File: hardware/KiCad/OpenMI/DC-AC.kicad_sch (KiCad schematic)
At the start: 41 parts, among them Q2 IPL60R125P7, Q3 IPL60R125P7, U1 IRS2304S

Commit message: chore: sync library
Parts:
- L10: footprint OpenCE:L_Radial_D10.5mm_P5.00mm_H14.5mm_Wuerth_1014 -> OpenCE:L_Radial_D10.0mm_P5.00mm_H14.0mm_Wuerth_1014
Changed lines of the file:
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@@
       (effects (font (size 1.27 1.27)))
     )
-    (property "Footprint" "OpenCE:L_Radial_D10.5mm_P5.00mm_H14.5mm_Wuerth_1014" (at 208.28 95.25 0)
+    (property "Footprint" "OpenCE:L_Radial_D10.0mm_P5.00mm_H14.0mm_Wuerth_1014" (at 208.28 95.25 0)
       (effects (font (size 1.27 1.27)) hide)
     )

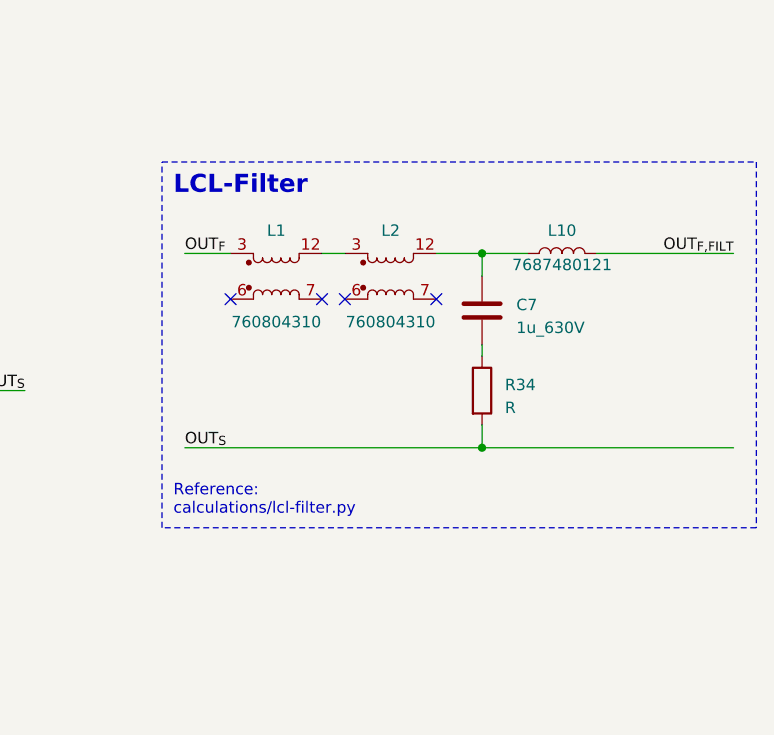
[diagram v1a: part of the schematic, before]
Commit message: feat(hw): Adds damping resistors to LCL-filter
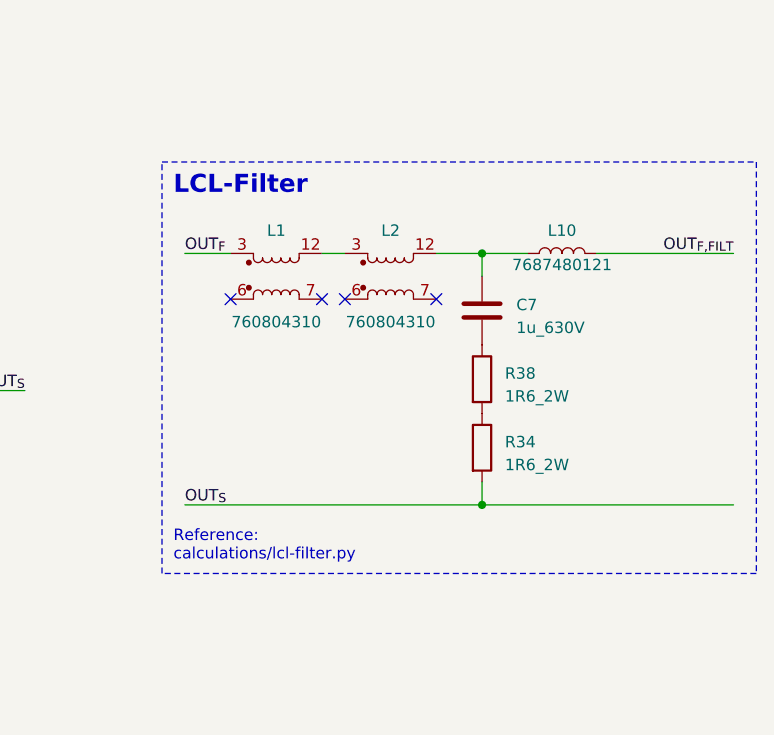
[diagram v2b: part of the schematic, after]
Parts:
- removed R34: R, symbol Device:R
- added R34, R38: 1R6_2W, Resistor_THT:R_Axial_DIN0411_L9.9mm_D3.6mm_P5.08mm_Vertical, symbol _R_Power:1R6_2W
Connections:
- net OUT_{S}: now also R34.2
- net at C7.2: now also R38.1
- new net: R34.1, R38.2
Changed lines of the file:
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@@
   (junction (at 135.89 50.8) (diameter 0) (color 0 0 0 0)
   )
-  (junction (at 199.39 116.84) (diameter 0) (color 0 0 0 0)
+  (junction (at 199.39 123.19) (diameter 0) (color 0 0 0 0)
   )
   (junction (at 93.98 97.79) (diameter 0) (color 0 0 0 0)
@@
     (stroke (width 0) (type default))
   )
-  (wire (pts (xy 166.37 116.84) (xy 199.39 116.84))
+  (wire (pts (xy 166.37 123.19) (xy 199.39 123.19))
     (stroke (width 0) (type default))
   )
@@
     (stroke (width 0) (type default))
   )
-  (wire (pts (xy 199.39 116.84) (xy 227.33 116.84))
+  (wire (pts (xy 199.39 123.19) (xy 227.33 123.19))
     (stroke (width 0) (type default))
   )
@@
     (stroke (width 0) (type default))
   )
-  (wire (pts (xy 199.39 114.3) (xy 199.39 116.84))
-    (stroke (width 0) (type default))
-  )
   (wire (pts (xy 109.22 160.02) (xy 109.22 158.75))
     (stroke (width 0) (type default))
@@
     (stroke (width 0) (type default))
   )
-  (wire (pts (xy 199.39 105.41) (xy 199.39 106.68))
-    (stroke (width 0) (type default))
-  )
   (wire (pts (xy 124.46 172.72) (xy 137.16 172.72))
     (stroke (width 0) (type default))
@@
   )
   (wire (pts (xy 93.98 172.72) (xy 93.98 171.45))
+    (stroke (width 0) (type default))
+  )
+  (wire (pts (xy 199.39 120.65) (xy 199.39 123.19))
     (stroke (width 0) (type default))
   )
@@
     (fill (type none))
   )
-  (rectangle (start 163.83 85.09) (end 229.87 125.73)
+  (rectangle (start 163.83 85.09) (end 229.87 130.81)
     (stroke (width 0) (type dash))
     (fill (type none))
@@
     (effects (font (size 2 2) bold) (justify left bottom))
   )
-  (text "Reference: \ncalculations/lcl-filter.py" (at 165.1 124.46 0)
+  (text "Reference: \ncalculations/lcl-filter.py" (at 165.1 129.54 0)
     (effects (font (size 1.27 1.27)) (justify left bottom))
   )
@@
     (effects (font (size 1.27 1.27) bold) (justify right bottom))
   )
-  (label "OUT_{S}" (at 166.37 116.84 0) (fields_autoplaced)
+  (label "OUT_{S}" (at 166.37 123.19 0) (fields_autoplaced)
     (effects (font (size 1.27 1.27)) (justify left bottom))
   )
@@
         (path "/2d959e19-1572-42a0-a8fd-da8463ad4e66/19323a41-9b99-4de4-bfae-f2f828815be3"
           (reference "R3") (unit 1)
-        )
-      )
-    )
-  )
-  (symbol (lib_id "Device:R") (at 199.39 110.49 0) (unit 1)
-    (in_bom yes) (on_board yes) (dnp no) (fields_autoplaced)
-    (property "Reference" "R34" (at 201.93 109.855 0)
-      (effects (font (size 1.27 1.27)) (justify left))
-    )
-    (property "Value" "R" (at 201.93 112.395 0)
-      (effects (font (size 1.27 1.27)) (justify left))
-    )
-    (property "Footprint" "" (at 197.612 110.49 90)
-      (effects (font (size 1.27 1.27)) hide)
-    )
-    (property "Datasheet" "~" (at 199.39 110.49 0)
-      (effects (font (size 1.27 1.27)) hide)
-    )
-    (pin "1")
-    (pin "2")
-    (instances
-      (project "OpenMI"
-        (path "/2d959e19-1572-42a0-a8fd-da8463ad4e66/19323a41-9b99-4de4-bfae-f2f828815be3"
-          (reference "R34") (unit 1)
         )
       )
@@
     )
   )
+  (symbol (lib_id "_R_Power:1R6_2W") (at 199.39 109.22 0) (unit 1)
+    (in_bom yes) (on_board yes) (dnp no) (fields_autoplaced)
+    (property "Reference" "R38" (at 201.93 108.585 0)
+      (effects (font (size 1.27 1.27)) (justify left))
+    )
+    (property "Value" "1R6_2W" (at 201.93 111.125 0)
+      (effects (font (size 1.27 1.27)) (justify left))
+    )
+    (property "Footprint" "Resistor_THT:R_Axial_DIN0411_L9.9mm_D3.6mm_P5.08mm_Vertical" (at 197.612 109.22 90)
+      (effects (font (size 1.27 1.27)) hide)
+    )
+    (property "Datasheet" "https://www.vishay.com/docs/28729/pr010203.pdf" (at 199.39 109.22 0)
+      (effects (font (size 1.27 1.27)) hide)
+    )
+    (property "MF" "Vishay" (at 199.39 109.22 0)
+      (effects (font (size 1.27 1.27)) hide)
+    )
+    (property "MPN" "PR02000201608JR500" (at 199.39 109.22 0)
+      (effects (font (size 1.27 1.27)) hide)
+    )
+    (property "OC_CONRAD" "" (at 199.39 109.22 0)
+      (effects (font (size 1.27 1.27)) hide)
+    )
+    (property "OC_FARNELL" "" (at 199.39 109.22 0)
+      (effects (font (size 1.27 1.27)) hide)
+    )
+    (property "OC_LCSC" "" (at 199.39 109.22 0)
+      (effects (font (size 1.27 1.27)) hide)
+    )
+    (property "OC_MOUSER" "594-5083NW1R600J" (at 199.39 109.22 0)
+      (effects (font (size 1.27 1.27)) hide)
+    )
+    (property "OC_REICHELT" "" (at 199.39 109.22 0)
+      (effects (font (size 1.27 1.27)) hide)
+    )
+    (pin "1")
+    (pin "2")
+    (instances
+      (project "OpenMI"
+        (path "/2d959e19-1572-42a0-a8fd-da8463ad4e66/19323a41-9b99-4de4-bfae-f2f828815be3"
+          (reference "R38") (unit 1)
+        )
+      )
+    )
+  )
   (symbol (lib_id "_Transistor_FET:IPL60R125P7") (at 125.73 101.6 0) (unit 1)
     (in_bom yes) (on_board yes) (dnp no) (fields_autoplaced)
@@
         )
       )
+    )
+  )
+  (symbol (lib_id "_R_Power:1R6_2W") (at 199.39 116.84 0) (unit 1)
+    (in_bom yes) (on_board yes) (dnp no)
+    (property "Reference" "R34" (at 201.93 116.205 0)
+      (effects (font (size 1.27 1.27)) (justify left))
+    )
+    (property "Value" "1R6_2W" (at 201.93 118.745 0)
+      (effects (font (size 1.27 1.27)) (justify left))
+    )
+    (property "Footprint" "Resistor_THT:R_Axial_DIN0411_L9.9mm_D3.6mm_P5.08mm_Vertical" (at 197.612 116.84 90)
+      (effects (font (size 1.27 1.27)) hide)
+    )
+    (property "Datasheet" "https://www.vishay.com/docs/28729/pr010203.pdf" (at 199.39 116.84 0)
+      (effects (font (size 1.27 1.27)) hide)
+    )
+    (property "MF" "Vishay" (at 199.39 116.84 0)
+      (effects (font (size 1.27 1.27)) hide)
+    )
+    (property "MPN" "PR02000201608JR500" (at 199.39 116.84 0)
+      (effects (font (size 1.27 1.27)) hide)
+    )
+    (property "OC_CONRAD" "" (at 199.39 116.84 0)
+      (effects (font (size 1.27 1.27)) hide)
+    )
+    (property "OC_FARNELL" "" (at 199.39 116.84 0)
+      (effects (font (size 1.27 1.27)) hide)
+    )
+    (property "OC_LCSC" "" (at 199.39 116.84 0)
+      (effects (font (size 1.27 1.27)) hide)
+    )
+    (property "OC_MOUSER" "594-5083NW1R600J" (at 199.39 116.84 0)
+      (effects (font (size 1.27 1.27)) hide)
+    )
+    (property "OC_REICHELT" "" (at 199.39 116.84 0)
+      (effects (font (size 1.27 1.27)) hide)
+    )
+    (pin "1")
+    (pin "2")
+    (instances
+      (project "OpenMI"
+        (path "/2d959e19-1572-42a0-a8fd-da8463ad4e66/19323a41-9b99-4de4-bfae-f2f828815be3"
+          (reference "R34") (unit 1)
+        )
+      )

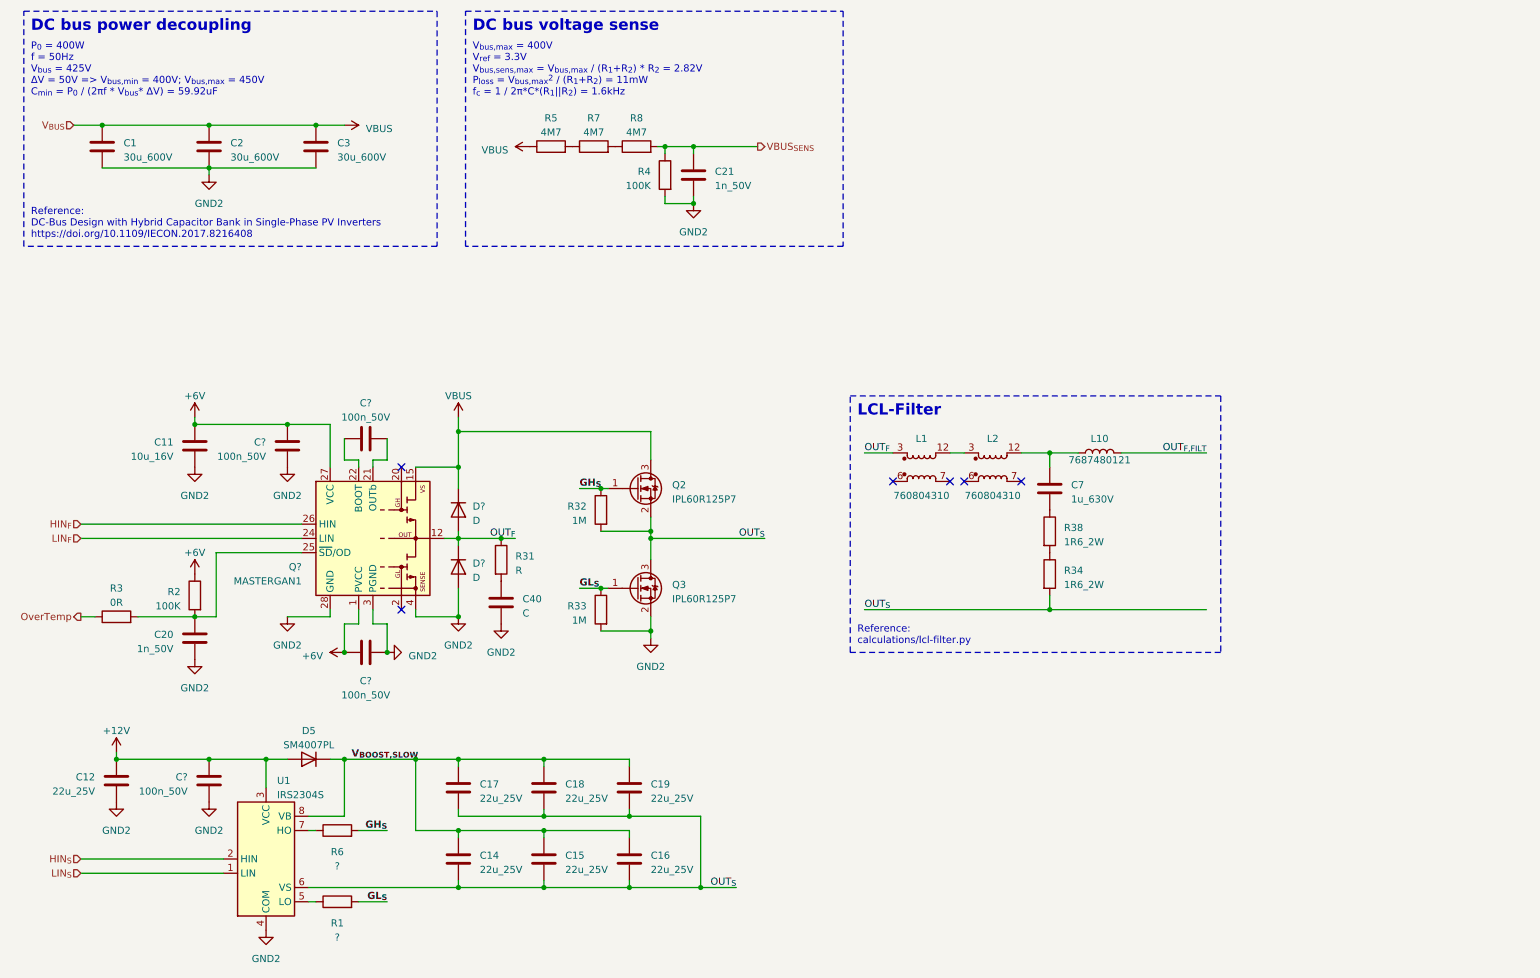
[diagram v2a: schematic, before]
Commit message: feat(hw): Adds draft of current sensing
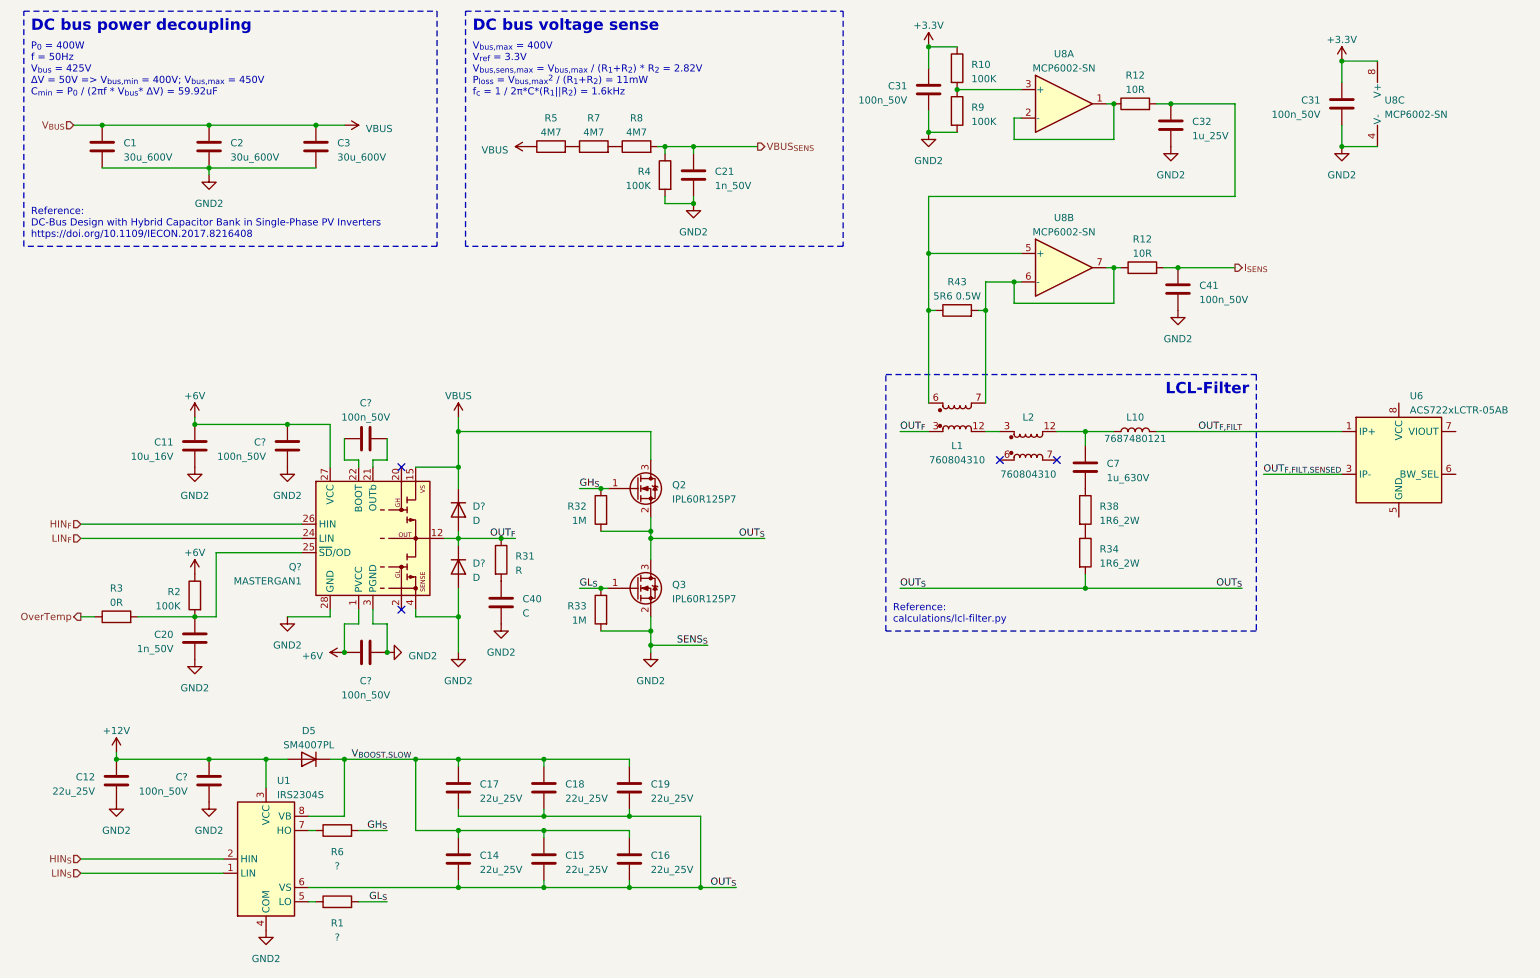
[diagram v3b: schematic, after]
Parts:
- added C31 (x2), C41: 100n_50V, Capacitor_SMD:C_0603_1608Metric, symbol _C_0603:100n_50V
- added C32: 1u_25V, Capacitor_SMD:C_0805_2012Metric, symbol _C_0805:1u_25V
- added R10, R9: 100K, Resistor_SMD:R_0603_1608Metric, symbol _R_0603:100K
- added R12 (x2): 10R, Resistor_SMD:R_0603_1608Metric, symbol _R_0603:10R
- added R43: 5R6 0.5W, symbol Device:R
- added U6: ACS722xLCTR-05AB, Package_SO:SOIC-8_3.9x4.9mm_P1.27mm, symbol Sensor_Current:ACS722xLCTR-05AB
- added U8: MCP6002-SN, Package_SO:SOIC-8_3.9x4.9mm_P1.27mm, symbol _Amplifier_Operational:MCP6002-SN
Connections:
- net GND: now also C31.2, C31.2, C32.2, C41.2, R9.2, U8.4 (V-)
- net OUT_{F,FILT}: now also U6.1 (IP+), U6.2 (IP+)
- net at L1.6: now also C32.1, R12.2, R43.1, U8.5 (+)
- net at L1.7: now also R12.1, R43.2, U8.6 (-), U8.7
- new net: R10.2, R9.1, U8.3 (+)
- new net: R12.1, U8.1, U8.2 (-)
- new net +3.3V: C31.1, C31.1, R10.1, U8.8 (V+)
- new net I_{SENS}: C41.1, R12.2
- new net OUT_{F,FILT,SENSED}: U6.3 (IP-), U6.4 (IP-)
- no-connect marks 6 -> 4
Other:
- moved on the sheet: C7, L1, L10, L2, R34, R38

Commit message: build(hw): Updates `_Transistor_FET:IPL60R125P7` from library
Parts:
- Q2, Q3: footprint Package_TO_SOT_SMD:PQFN_8x8 -> OpenCE:Q_ThinPAK_8x8_NMOS_GSD
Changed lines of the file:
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@@
       (effects (font (size 1.27 1.27)) (justify left))
     )
-    (property "Footprint" "Package_TO_SOT_SMD:PQFN_8x8" (at 130.81 116.84 0)
+    (property "Footprint" "OpenCE:Q_ThinPAK_8x8_NMOS_GSD" (at 130.81 116.84 0)
       (effects (font (size 1.27 1.27)) hide)
     )
@@
       (effects (font (size 1.27 1.27)) (justify left))
     )
-    (property "Footprint" "Package_TO_SOT_SMD:PQFN_8x8" (at 130.81 99.06 0)
-      (effects (font (size 1.27 1.27)) hide)
-    )
+    (property "Footprint" "OpenCE:Q_ThinPAK_8x8_NMOS_GSD" (at 130.81 99.06 0)
+      (effects (font (size 1.27 1.27)) hide)
+    )

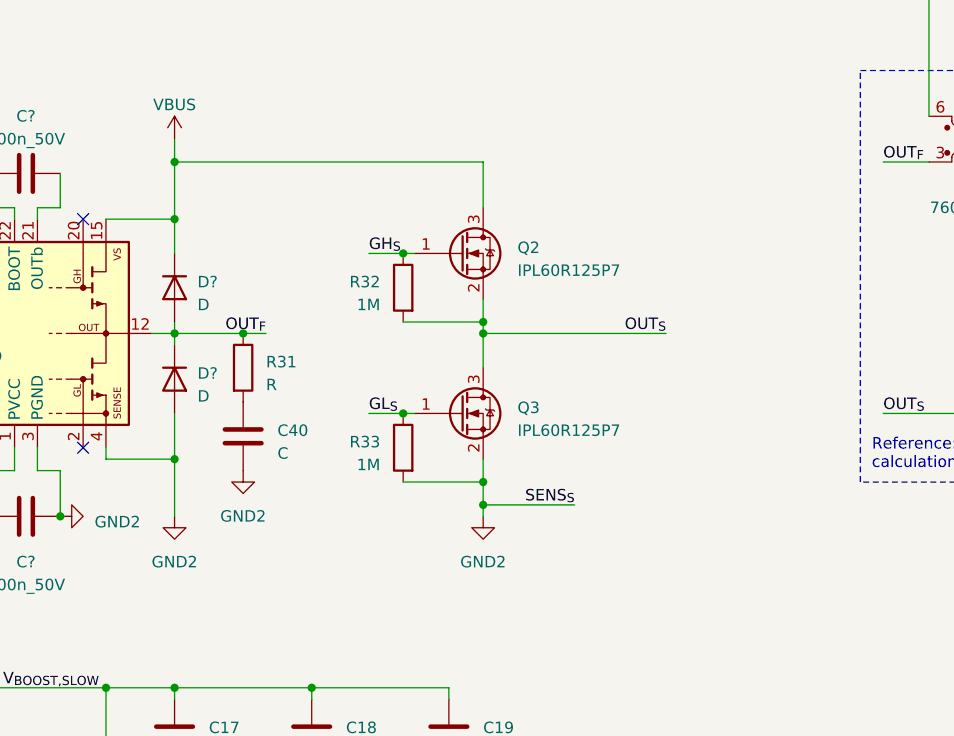
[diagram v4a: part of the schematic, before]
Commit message: feat(hw): Adds freewheeling diodes to MASTERGAN
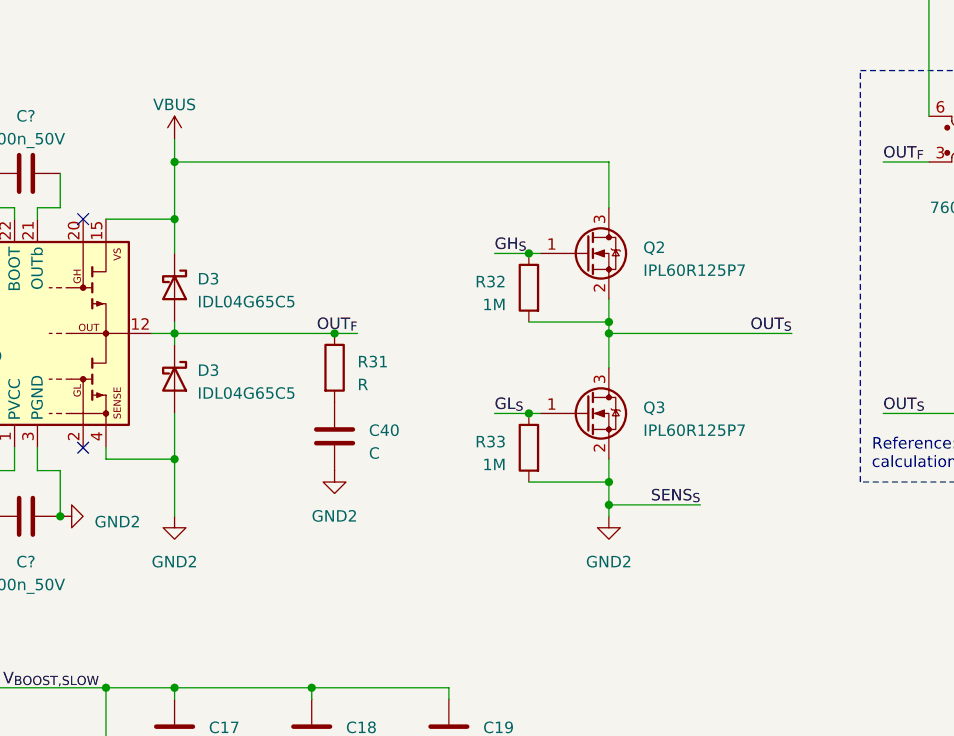
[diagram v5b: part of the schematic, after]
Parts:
- removed D? (x2): D, symbol Device:D
- added D3 (x2): IDL04G65C5, OpenCE:D_ThinPAK_8x8, symbol _Diode_Schottky:IDL04G65C5
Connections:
- net GND: now also D3.2 (A)
- net OUT_{F}: now also D3.1 (K), D3.2 (A)
- net VBUS: now also D3.1 (K)
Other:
- moved on the sheet: C40, Q2, Q3, R31, R32, R33
